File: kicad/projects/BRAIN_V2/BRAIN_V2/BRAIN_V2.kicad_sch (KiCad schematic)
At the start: 64 parts, among them J1 Conn_ARM_JTAG_SWD_10, J2 UART, J3 USB_C_Receptacle_USB2.0_16P, J4 CONN_2x1, J5 I2C, J6 Conn_02x11_Odd_Even, J7 Conn_02x04_Odd_Even, J8 Conn_02x06_Odd_Even, Q1 BC847, SW1 TL3342F450QG, U1 24LC512, U3 AP2112K-3.3, U4 AP2112K-3.3, U73 STM32L433CCTx, Y1 NX3215SA-32.768KHZ-EXS00A-MU0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

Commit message: brain v2, all components placed?
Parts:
- removed J4: CONN_2x1, Connector_JST:JST_EH_B2B-EH-A_1x02_P2.50mm_Vertical, symbol Connector_Generic:Conn_01x02
- added J9: USB_C_Receptacle_USB2.0_16P, Connector_USB:USB_C_Receptacle_XKB_U262-16XN-4BVC11, symbol Connector:USB_C_Receptacle_USB2.0_16P
- D2, D4: now not fitted
- J2: footprint Connector_PinHeader_2.54mm:PinHeader_1x04_P2.54mm_Horizontal -> Connector_PinHeader_2.54mm:PinHeader_1x04_P2.54mm_Vertical
- J3: footprint Connector_USB:USB_C_Receptacle_GCT_USB4105-xx-A_16P_TopMnt_Horizontal -> Connector_USB:USB_C_Receptacle_XKB_U262-16XN-4BVC11; MP XKB Connection U262-161N-4BS165 -> U262-161N-4BS165
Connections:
- net HWREV3 is gone; now on net HWREV2: U73.44 (PH3)
- net +3V3: no longer J6.11 (Pin_11), J6.12 (Pin_12), J6.9 (Pin_9)
- net 3V3_OUT: now also J6.11 (Pin_11), J6.12 (Pin_12), J6.9 (Pin_9)
- net FBK_3V3_SENSORS: no longer J6.14 (Pin_14)
- net GND: now also D6.1 (K), D8.1 (K), D9.1 (K), J9.A1 (GND), J9.A12 (GND), J9.B1 (GND), J9.B12 (GND), J9.S1 (SHIELD); no longer R11.2, R12.2, R15.2
- net HWREV1: now also R20.2, R21.1
- net LED_ALIVE: now also R11.1; no longer D6.2 (A)
- net LED_USER1: now also R12.1; no longer D8.2 (A)
- net LED_USER2: now also R15.1; no longer D9.2 (A)
- net at D2.1 (A1), D4.2 (A): now also J9.A4 (VBUS), J9.A9 (VBUS), J9.B4 (VBUS), J9.B9 (VBUS)
- new net: D6.2 (A), R11.2
- new net: D8.2 (A), R12.2
- new net: D9.2 (A), R15.2
- new net FBK_3V3_SENSORS_EXT: J6.14 (Pin_14)
- no-connect marks 5 -> 13
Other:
- moved on the sheet: D5, D6, D7, D8, D9, J3, R10, R11, R12, R15, R24, R9

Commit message: brain v2 connections
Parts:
- removed D2: PESD5V0L2BT, PCM_Package_TO_SOT_SMD_AKL:SOT-23, symbol Diode_TVS_AKL:PESD5V0L2BT
- removed D7: TVS3V3L4U, PCM_Package_SO_AKL:TSOP-6_1.65x3.05mm_P0.95mm, symbol Diode_TVS_AKL:TVS3V3L4U
- added D10: PESD5V0L2BT, PCM_Package_TO_SOT_SMD_AKL:SOT-23, symbol PCM_Diode_TVS_AKL:PESD5V0L2BT
- added D2: TVS3V3L4U, PCM_Package_SO_AKL:TSOP-6_1.65x3.05mm_P0.95mm, symbol PCM_Diode_TVS_AKL:TVS3V3L4U
- added R16, R17: 5.1k, Resistor_SMD:R_0805_2012Metric_Pad1.20x1.40mm_HandSolder, symbol Device:R
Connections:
- net GND: now also D10.3 (Com), R16.2, R17.2
- net SIG1: now also R6.1; no longer R3.1
- net SIG2: now also R5.1; no longer R4.1
- net SIG3: now also R4.1; no longer R5.1
- net SIG4: now also R3.1; no longer R6.1
- net USB_N: now also D2.1 (L1), D2.4 (L3)
- net USB_P: now also D2.3 (L2), D2.6 (L4)
- net at D4.2 (A), J9.A4 (VBUS), J9.A9 (VBUS)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: now also D10.1 (A1)
- net at J9.A5 (CC1): now also R16.1
- net at J9.B5 (CC2): now also R17.1
- net 5V_USB: no longer names the net of D5.2 (A), J3.A4 (VBUS), J3.A9 (VBUS), J3.B4 (VBUS), J3.B9 (VBUS)
- net 5V_USB: now also D10.2 (A2)
- net FBK_3V3_SENSORS_EXT: no longer names the net of J6.14 (Pin_14)
- no-connect marks 13 -> 12
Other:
- moved on the sheet: C1, C10, C11, C12, C13, C14, C15, C16, C2, C3, C4, C5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

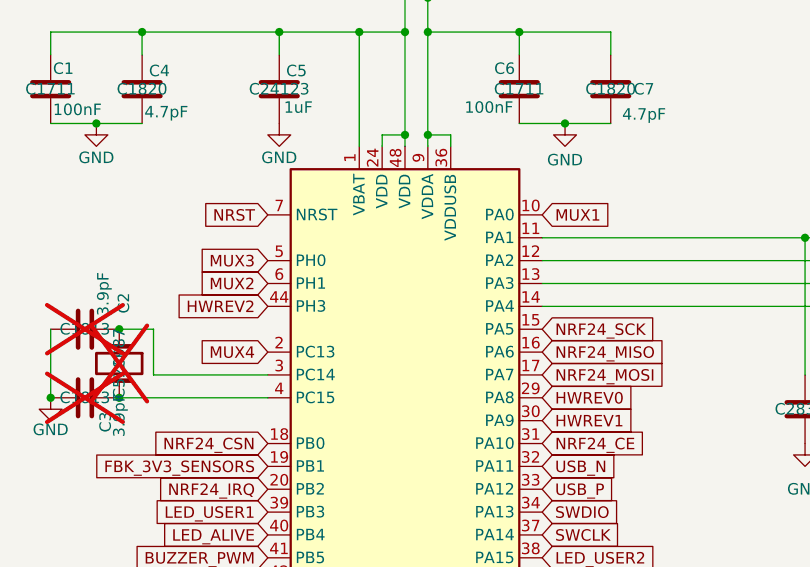
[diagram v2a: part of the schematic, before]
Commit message: brain v2 connections
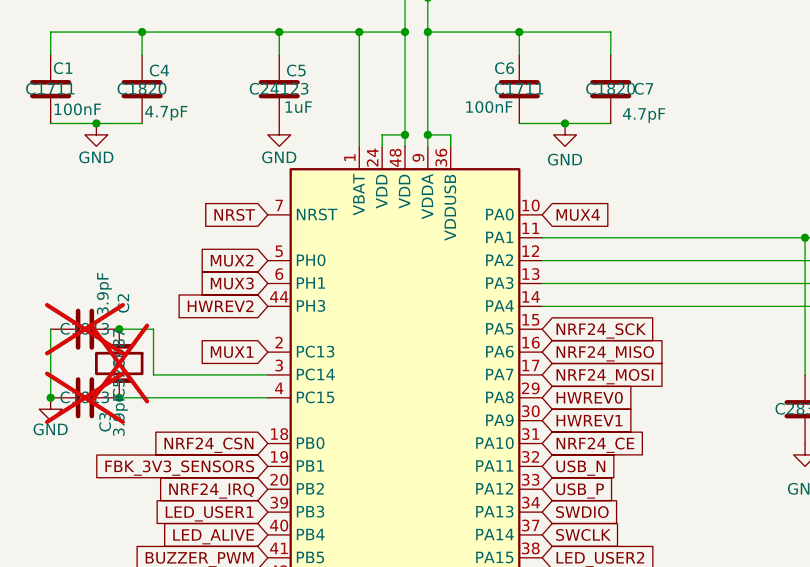
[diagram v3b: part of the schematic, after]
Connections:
- net MUX1: now also U73.2 (PC13); no longer U73.10 (PA0)
- net MUX2: now also U73.5 (PH0); no longer U73.6 (PH1)
- net MUX3: now also U73.6 (PH1); no longer U73.5 (PH0)
- net MUX4: now also U73.10 (PA0); no longer U73.2 (PC13)

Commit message: hw revisions and versions in schematic and pins
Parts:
- removed C2, C3: 3.9pF, Capacitor_SMD:C_0805_2012Metric_Pad1.18x1.45mm_HandSolder, symbol Device:C
- removed J8: Conn_02x06_Odd_Even, Connector_PinHeader_2.54mm:PinHeader_2x06_P2.54mm_Vertical_SMD, symbol Connector_Generic:Conn_02x06_Odd_Even
- removed R24, R25: 10k, Resistor_SMD:R_0805_2012Metric_Pad1.20x1.40mm_HandSolder, symbol Device:R
- removed Y1: NX3215SA-32.768KHZ-EXS00A-MU00525, PCM_Crystal_AKL:Crystal_SMD_MicroCrystal_CC7V-T1A-2Pin_3.2x1.5mm_HandSoldering, symbol Device:Crystal
- added J4: Conn_02x03_Odd_Even, Connector_PinHeader_2.54mm:PinHeader_2x03_P2.54mm_Vertical_SMD, symbol Connector_Generic:Conn_02x03_Odd_Even
- added R18, R19, R28, R29, R30: 10k, Resistor_SMD:R_0805_2012Metric_Pad1.20x1.40mm_HandSolder, symbol Device:R
- added R31: 47k, Resistor_SMD:R_0805_2012Metric_Pad1.20x1.40mm_HandSolder, symbol Device:R
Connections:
- net +3V3: now also J4.1 (Pin_1), J4.2 (Pin_2)
- net 3V3_OUT: now also J6.13 (Pin_13), J6.14 (Pin_14), J6.7 (Pin_7), R18.2, R19.1, R28.1, R29.1, R30.1; no longer J6.11 (Pin_11), J6.12 (Pin_12), J6.9 (Pin_9)
- net EXPANSION0: now also J4.3 (Pin_3)
- net EXPANSION1: now also J4.5 (Pin_5)
- net FBK_3V3_SENSORS: now also J6.16 (Pin_16), U73.10 (PA0), R31.1; no longer R26.1, R27.1, U73.19 (PB1)
- net GND: now also J6.15 (Pin_15), J6.18 (Pin_18), J6.19 (Pin_19), J4.4 (Pin_4), J4.6 (Pin_6), R31.2; no longer J6.13 (Pin_13), J6.16 (Pin_16), J6.17 (Pin_17), J6.20 (Pin_20), J6.21 (Pin_21), J6.4 (Pin_4), J6.5 (Pin_5), J6.8 (Pin_8)
- net MUX1: now also J6.9 (Pin_9); no longer J6.3 (Pin_3)
- net MUX2: now also J6.10 (Pin_10), U73.3 (PC14); no longer J6.6 (Pin_6), U73.5 (PH0)
- net MUX3: now also J6.11 (Pin_11), U73.4 (PC15); no longer J6.7 (Pin_7), U73.6 (PH1)
- net MUX4: now also J6.12 (Pin_12), U73.5 (PH0); no longer J6.10 (Pin_10), U73.10 (PA0)
- net SIG2: now also J6.17 (Pin_17); no longer J6.15 (Pin_15)
- net SIG3: now also J6.20 (Pin_20); no longer J6.18 (Pin_18)
- net SIG4: now also J6.21 (Pin_21); no longer J6.19 (Pin_19)
- net EXPANSION2 renamed SENSORS_HW_ID0
- net SENSORS_HW_ID0: now also J6.5 (Pin_5), R28.2
- net EXPANSION3 renamed SENSORS_HW_ID1
- net SENSORS_HW_ID1: now also J6.6 (Pin_6), R29.2
- net EXPANSION4 renamed SENSORS_HW_ID2
- net SENSORS_HW_ID2: now also J6.8 (Pin_8), R30.2
- net HWREV2 renamed SENSORS_REV1
- net SENSORS_REV1: now also J6.4 (Pin_4), R19.2
- new net FBK_3V3_BRAIN: R26.1, R27.1, U73.19 (PB1)
- new net SENSORS_REV0: J6.3 (Pin_3), R18.1, U73.6 (PH1)
- no-connect marks 12 -> 11
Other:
- moved on the sheet: J2, J5, J6, J7, R21, R23

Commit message: sensors matrix with jlcpcb
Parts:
- R13: now in the parts list
- R2: MANUFACTURER (none) -> RC0805FR-0747KL
- R31: LCSC p/n (none) -> C126351; MANUFACTURER (none) -> RC0805FR-0747KL; shop (none) -> https://www.lcsc.com/product-detail/Chip-Resistor-Surface-M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
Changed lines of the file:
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@@
 		)
 	)
-	(global_label "SENSORS_HW_ID0"
-		(shape input)
-		(at 369.57 129.54 0)
-		(fields_autoplaced yes)
-		(effects
-			(font
-				(size 1.27 1.27)
-			)
-			(justify left)
-		)
-		(property "Intersheetrefs" "${INTERSHEET_REFS}"
-			(at 389.0651 129.54 0)
-			(effects
-				(font
-					(size 1.27 1.27)
-				)
-				(justify left)
-				(hide yes)
-			)
-		)
-	)
 	(global_label "3V3_OUT"
 		(shape input)
@@
 			)
 		)
-		(property "Datasheet" "https://www.lcsc.com/datasheet/lcsc_datasheet_2412232100_YAGEO-RC0805FR-0710KL_C84376.pdf"
+		(property "Datasheet" "https://www.lcsc.com/datasheet/C126351.pdf?spm=wm.sxq.inf.ggs&lcsc_vid=E1APAwdRQ1VeXlFQFANfA11XFQQPUVdeQlJeXgIEEgAxVlNfRVBbUVJVQlhdVjtW"
 			(at 76.2 262.89 0)
 			(effects
@@
 			)
 		)
-		(property "LCSC p/n" ""
+		(property "LCSC p/n" "C126351"
 			(at 78.74 264.1599 0)
 			(effects
@@
 			)
 		)
-		(property "shop" ""
+		(property "shop" "https://www.lcsc.com/product-detail/Chip-Resistor-Surface-Mount_YAGEO-RC0805FR-0747KL_C126351.html"
+			(at 76.2 262.89 0)
+			(effects
+				(font
+					(size 1.27 1.27)
+				)
+				(hide yes)
+			)
+		)
+		(property "MANUFACTURER" "RC0805FR-0747KL"
 			(at 76.2 262.89 0)
 			(effects
@@
 		(unit 1)
 		(exclude_from_sim no)
-		(in_bom no)
+		(in_bom yes)
 		(on_board yes)
 		(dnp yes)
@@
 			)
 		)
-		(property "Datasheet" "https://www.lcsc.com/datasheet/lcsc_datasheet_2304140030_YAGEO-RC0805FR-0747KL_C126351.pdf"
+		(property "Datasheet" "https://www.lcsc.com/datasheet/C126351.pdf?spm=wm.sxq.inf.ggs&lcsc_vid=E1APAwdRQ1VeXlFQFANfA11XFQQPUVdeQlJeXgIEEgAxVlNfRVBbUVJVQlhdVjtW"
 			(at 109.22 124.46 0)
 			(effects
@@
 			(at 109.22 124.46 0)
 			(effects
+				(font
+					(size 1.27 1.27)
+				)
+				(hide yes)
+			)
+		)
+		(property "MANUFACTURER" "RC0805FR-0747KL"
+			(at 109.22 124.46 0)
+			(effects
